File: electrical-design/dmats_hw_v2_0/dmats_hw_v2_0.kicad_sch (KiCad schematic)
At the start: 9 parts, among them J3 Hall_Effect_Sensor_Mod, J4 Hall_Effect_Sensor_Mod, M1 Motor_DC, SW1 RotaryEncoder, U1 ABX00042

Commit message: v2 of circuit for PCB
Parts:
- removed J3, J4: Hall_Effect_Sensor_Mod, symbol Connector:Conn_01x04_Pin
- added U2 (x2): A1324, Package_TH_SIP:SIP-3, symbol custom:A132x
- BT1, BT2, BT3: value Battery_Cell -> 3V7 LI-ION
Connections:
- net +3.3V: now also U1.JD3 (+3V3)
- net +5V: now also U1.JD1 (+5V), U2.1 (VCC), U2.1 (VCC)
- net GND: now also U1.JD4 (GND_2), U2.3 (GND), U2.3 (GND)
- net M1: now also M1.1 (+); no longer M1.2 (-)
- net M2: now also M1.2 (-); no longer M1.1 (+)
- net C1: no longer names the net of U1.JA9 (D0)
- net C1: no longer SW1.C (C1)
- net C2: no longer names the net of U1.JA10 (D1)
- net C2: no longer SW1.B (C2)
- net HES_A1 renamed HES_OUT1
- net HES_OUT1: now also U2.2 (VOUT)
- net HES_A2 renamed HES_OUT2
- net HES_OUT2: now also U2.2 (VOUT)
- net HES_D1 renamed FAULT
- net HES_D2 renamed BLO
- net IN1 renamed AHI
- net IN2 renamed BHI
- net PWM_A renamed ALO
- new net ENC_A: SW1.B (C2)
- new net ENC_B: SW1.C (C1)
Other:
- note added: "5V over 3V3 to give better noise margin"
- note added: "A1324 chosen over A1325, A1326 for it's higher sensivity, better for yes/no sensing"
- moved on the sheet: BT1, BT2, BT3, M1, SW1, U1C, U4

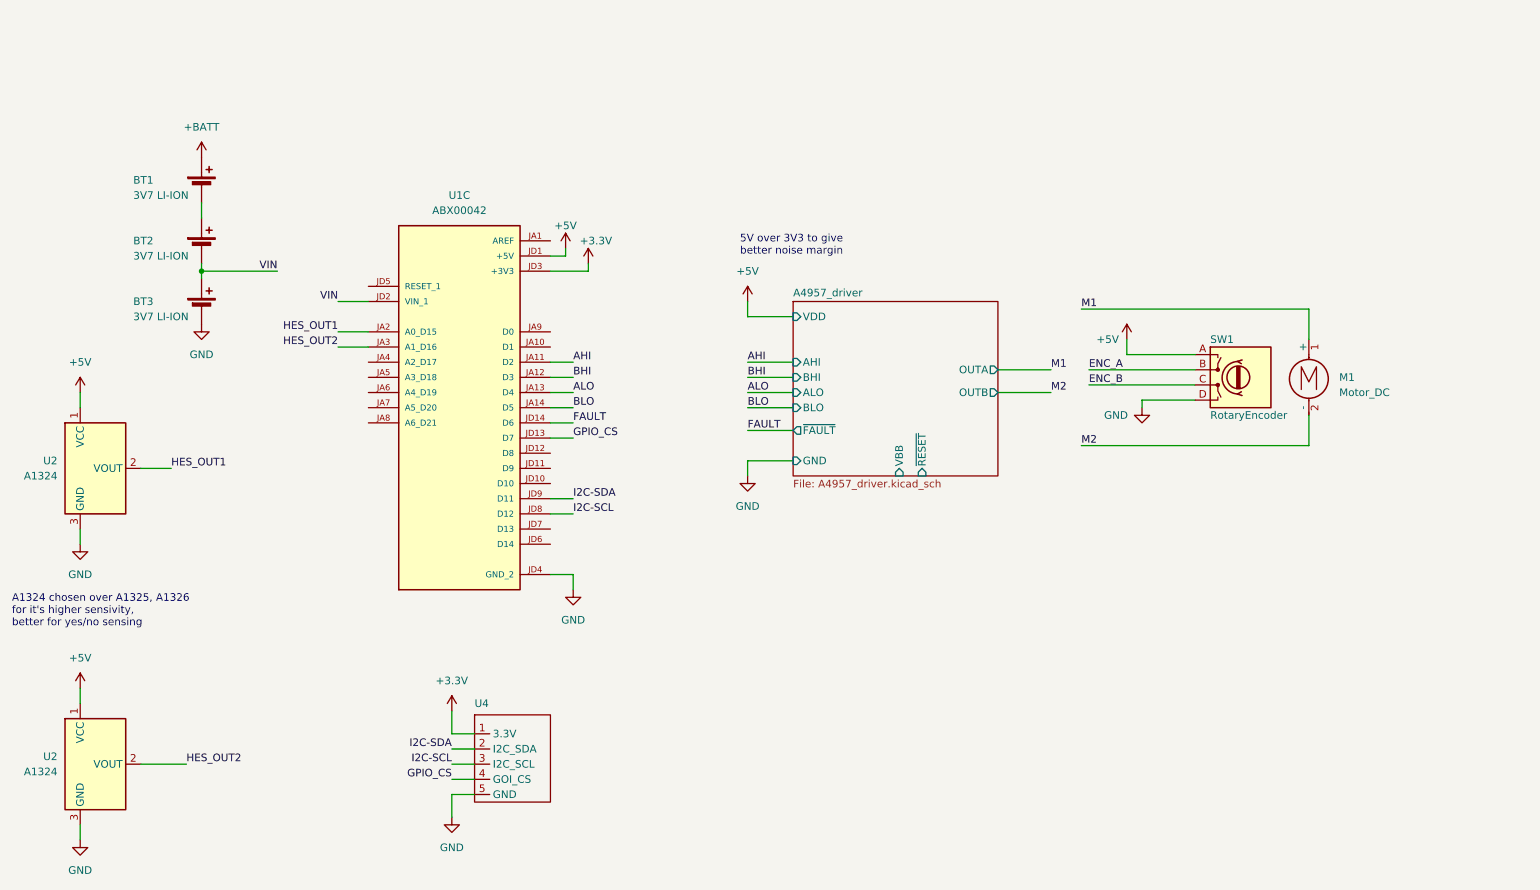
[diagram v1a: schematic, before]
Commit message: created all PCB footprints
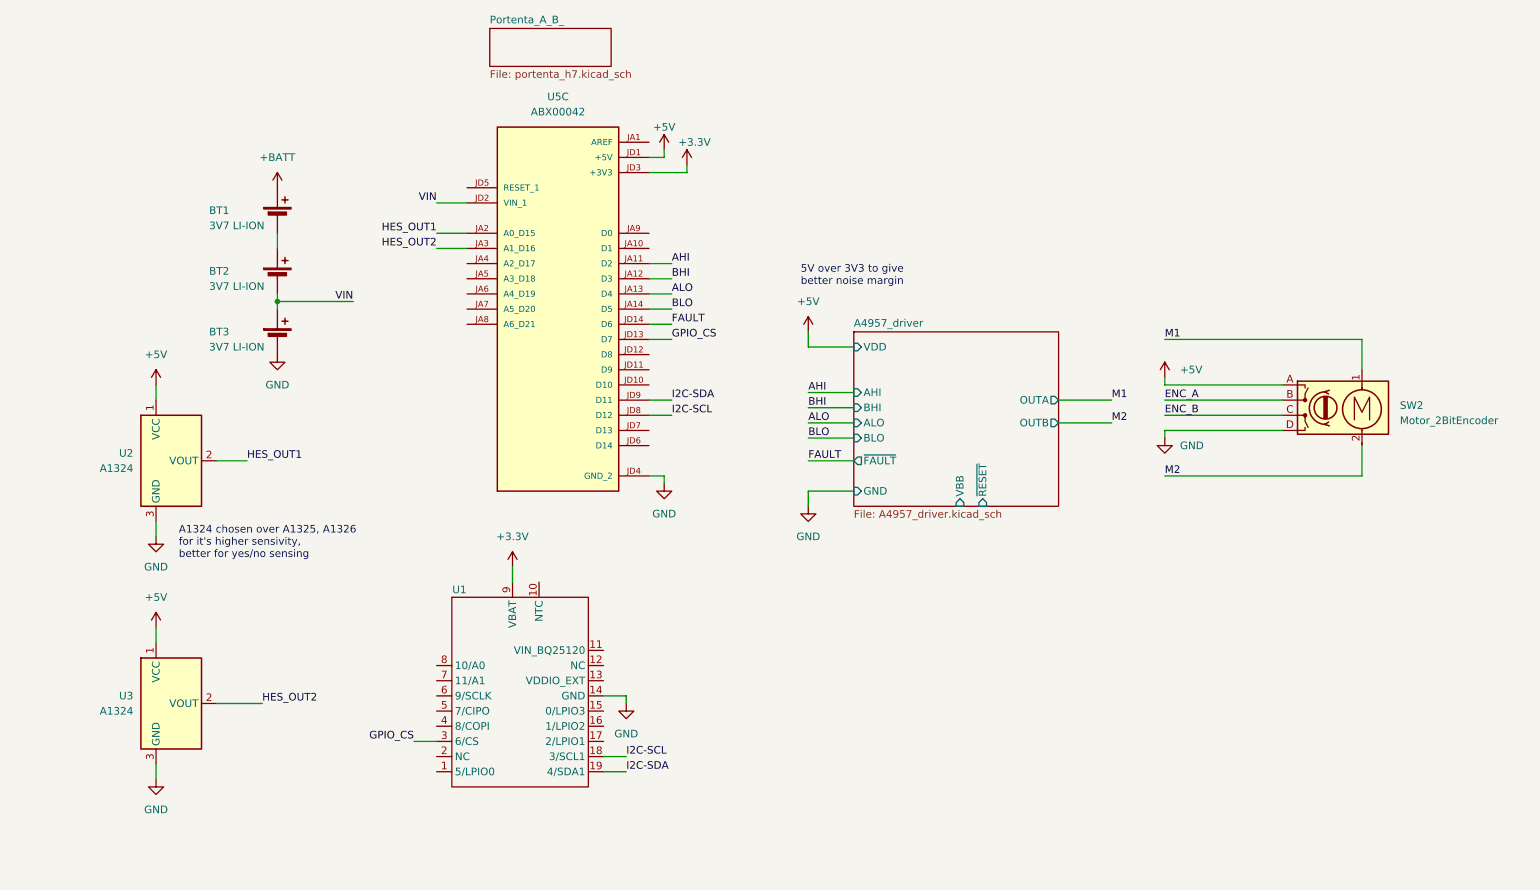
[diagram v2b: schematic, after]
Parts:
- removed M1: Motor_DC, symbol Motor:Motor_DC
- removed SW1: RotaryEncoder, symbol Device:RotaryEncoder
- removed U1: ABX00042, ABX00042:MODULE_ABX00042, symbol ABX00042:ABX00042
- removed U4: ~, symbol custom:NICLA_SENSE_ME
- added SW2: Motor_2BitEncoder, Resistor_SMD:R_0603_1608Metric, symbol DMATS_capstone:Motor_2BitEncoder
- added U1: ~, DMATS_capstone:ARDUINO_NICLA, symbol DMATS_capstone:Nicla_Sense_ME
- added U5: ABX00042, DMATS_capstone:MODULE_ABX00042, symbol DMATS_capstone:ABX00042
- renumbered U2 to U3
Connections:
- net +3.3V: now also U1.9 (VBAT), U5.JD3 (+3V3)
- net +5V: now also SW2.A (VCC), U5.JD1 (+5V)
- net AHI: now also U5.JA11 (D2)
- net ALO: now also U5.JA13 (D4)
- net BHI: now also U5.JA12 (D3)
- net BLO: now also U5.JA14 (D5)
- net ENC_A: now also SW2.B (C2)
- net ENC_B: now also SW2.C (C1)
- net FAULT: now also U5.JD14 (D6)
- net GND: now also SW2.D (GND), U1.14 (GND), U5.JD4 (GND_2)
- net GPIO_CS: now also U1.3 (6/CS), U5.JD13 (D7)
- net HES_OUT1: now also U5.JA2 (A0_D15)
- net HES_OUT2: now also U5.JA3 (A1_D16)
- net I2C-SCL: now also U1.18 (3/SCL1), U5.JD8 (D12)
- net I2C-SDA: now also U1.19 (4/SDA1), U5.JD9 (D11)
- net M1: now also SW2.1 (+)
- net M2: now also SW2.2 (-)
- net VIN: now also U5.JD2 (VIN_1)
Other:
- added sheet Portenta_A_B_ (portenta_h7.kicad_sch)
- moved on the sheet: BT1, BT2, BT3, U2, U3

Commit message: bulk of PCB design layout complete
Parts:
- removed U5: ABX00042, DMATS_capstone:MODULE_ABX00042, symbol DMATS_capstone:ABX00042
- added U4: ABX00042, DMATS_capstone:MODULE_ABX00042, symbol DMATS_capstone:ABX00042
- BT1, BT2, BT3: footprint (none) -> Battery:BatteryHolder_Keystone_1042_1x18650
- SW2: footprint Resistor_SMD:R_0603_1608Metric -> Connector_JST:JST_PH_B6B-PH-K_1x06_P2.00mm_Vertical
- U2, U3: footprint Package_TH_SIP:SIP-3 -> Connector_JST:JST_EH_S3B-EH_1x03_P2.50mm_Horizontal
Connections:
- net +3.3V: now also U4.JD3 (+3V3)
- net +5V: now also SW2.2 (VCC), U4.JD1 (+5V); no longer SW2.A (VCC)
- net AHI: now also U4.JA11 (D2)
- net ALO: now also U4.JA13 (D4)
- net BHI: now also U4.JA12 (D3)
- net BLO: now also U4.JA14 (D5)
- net ENC_A: now also SW2.3 (C2); no longer SW2.B (C2)
- net ENC_B: now also SW2.4 (C1); no longer SW2.C (C1)
- net FAULT: now also U4.JD14 (D6)
- net GND: now also SW2.5 (GND), U4.JD4 (GND_2); no longer SW2.D (GND)
- net GPIO_CS: now also U4.JD13 (D7)
- net HES_OUT1: now also U4.JA2 (A0_D15)
- net HES_OUT2: now also U4.JA3 (A1_D16)
- net I2C-SCL: now also U4.JD8 (D12)
- net I2C-SDA: now also U4.JD9 (D11)
- net M2: now also SW2.6 (M2); no longer SW2.2 (-)
- net VIN: now also U4.JD2 (VIN_1)
- new net: U4.J2_11 (NC_1), U4.J2_13 (NC_1), U4.J2_15 (NC_1), U4.J2_17 (NC_1), U4.J2_19 (NC_1), U4.J2_21 (NC_1), U4.J2_29 (NC_1), U4.J2_30 (NC_1), U4.J2_31 (NC_1), U4.J2_32 (NC_1), U4.J2_35 (NC_1), U4.J2_37 (NC_1), U4.J2_39 (NC_1), U4.J2_41 (NC_1), U4.J2_55 (NC_1), U4.J2_9 (NC_1)
- new net: U4.J2_23 (VCC/+3V3), U4.J2_43 (VCC/+3V3), U4.J2_69 (VCC/+3V3)
- new net: U4.J2_24 (GND_1), U4.J2_33 (GND_1), U4.J2_44 (GND_1), U4.J2_57 (GND_1), U4.J2_70 (GND_1)
- new net: U4.J1_11 (NC), U4.J1_13 (NC), U4.J1_15 (NC), U4.J1_2 (NC), U4.J1_24 (NC), U4.J1_30 (NC), U4.J1_4 (NC), U4.J1_50 (NC), U4.J1_52 (NC), U4.J1_6 (NC), U4.J1_67 (NC), U4.J1_69 (NC), U4.J1_70 (NC), U4.J1_71 (NC), U4.J1_74 (NC), U4.J1_76 (NC), U4.J1_78 (NC), U4.J1_8 (NC), U4.J1_80 (NC), U4.J1_9 (NC)
- new net: U4.J1_21 (VIN), U4.J1_32 (VIN), U4.J1_41 (VIN), U4.J1_48 (VIN)
- new net: U4.J1_22 (GND), U4.J1_31 (GND), U4.J1_42 (GND), U4.J1_47 (GND), U4.J1_54 (GND)
- new net: U4.J1_53 (VSYS), U4.J1_64 (VSYS)
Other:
- removed sheet Portenta_A_B_

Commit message: completed motor driver PCB
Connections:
- net +BATT: now also BT2.1 (+); no longer BT1.1 (+)
- net ALO: now also U4.JA12 (D3); no longer U4.JA13 (D4)
- net BHI: now also U4.JA13 (D4); no longer U4.JA12 (D3)
- net FAULT: now also U4.JA10 (D1); no longer U4.JD14 (D6)
- net VIN: now also BT1.2 (-); no longer BT2.2 (-)
- new net: BT1.1 (+), BT2.2 (-)
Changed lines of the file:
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@@
+    (stroke (width 0.25) (type default))
+  )
+  (wire (pts (xy 144.78 81.28) (xy 144.78 91.44))
     (stroke (width 0.25) (type default))
   )
   (wire (pts (xy 128.27 110.49) (xy 128.27 109.22))
+    (stroke (width 0.25) (type default))
+  )
+  (wire (pts (xy 144.78 91.44) (xy 160.02 91.44))
     (stroke (width 0.25) (type default))
   )
@@
     (stroke (width 0.25) (type default))
   )
-  (wire (pts (xy 125.73 83.82) (xy 129.54 83.82))
-    (stroke (width 0.25) (type default))
-  )
   (wire (pts (xy 43.18 93.98) (xy 43.18 96.52))
     (stroke (width 0.25) (type default))
@@
     (stroke (width 0.25) (type default))
   )
+  (wire (pts (xy 125.73 71.12) (xy 129.54 71.12))
+    (stroke (width 0.25) (type default))
+  )
   (wire (pts (xy 86.36 153.67) (xy 90.17 153.67))
     (stroke (width 0.25) (type default))
@@
     (effects (font (size 1.27 1.27)) (justify left bottom))
   )
-  (label "BHI" (at 129.54 76.2 0) (fields_autoplaced)
-    (effects (font (size 1.27 1.27)) (justify left bottom))
-  )
   (label "M2" (at 212.09 109.22 0) (fields_autoplaced)
     (effects (font (size 1.27 1.27)) (justify left bottom))
@@
     (effects (font (size 1.27 1.27)) (justify right bottom))
   )
-  (label "FAULT" (at 129.54 83.82 0) (fields_autoplaced)
-    (effects (font (size 1.27 1.27)) (justify left bottom))
-  )
   (label "HES_OUT2" (at 60.96 147.32 0) (fields_autoplaced)
     (effects (font (size 1.27 1.27)) (justify left bottom))
   )
   (label "FAULT" (at 152.4 106.68 0) (fields_autoplaced)
+    (effects (font (size 1.27 1.27)) (justify left bottom))
+  )
+  (label "FAULT" (at 129.54 71.12 0) (fields_autoplaced)
     (effects (font (size 1.27 1.27)) (justify left bottom))
   )
@@
     (effects (font (size 1.27 1.27)) (justify left bottom))
   )
+  (label "BHI" (at 129.54 78.74 0) (fields_autoplaced)
+    (effects (font (size 1.27 1.27)) (justify left bottom))
+  )
   (label "I2C-SCL" (at 121.92 156.21 0) (fields_autoplaced)
     (effects (font (size 1.27 1.27)) (justify left bottom))
@@
     (effects (font (size 1.27 1.27)) (justify left bottom))
   )
-  (label "ALO" (at 129.54 78.74 0) (fields_autoplaced)
+  (label "ALO" (at 129.54 76.2 0) (fields_autoplaced)
     (effects (font (size 1.27 1.27)) (justify left bottom))
   )
@@
     )
   )
+  (symbol (lib_id "Device:Battery_Cell") (at 63.5 66.04 0) (unit 1)
+    (in_bom yes) (on_board yes) (dnp no)
+    (property "Reference" "BT2" (at 52.07 64.77 0)
+      (effects (font (size 1.27 1.27)) (justify left))
+    )
+    (property "Value" "3V7 LI-ION" (at 52.07 67.31 0)
+      (effects (font (size 1.27 1.27)) (justify left))
+    )
+    (property "Footprint" "Battery:BatteryHolder_Keystone_1042_1x18650" (at 63.5 64.516 90)
+      (effects (font (size 1.27 1.27)) hide)
+    )
+    (property "Datasheet" "~" (at 63.5 64.516 90)
+      (effects (font (size 1.27 1.27)) hide)
+    )
+    (pin "1")
+    (pin "2")
+    (instances
+      (project "dmats_hw_v2_0"
+        (path "/47782a9e-3834-4fdd-a08d-6cefd0e2f2ff"
+          (reference "BT2") (unit 1)
+        )
+      )
+    )
+  )
   (symbol (lib_id "power:+5V") (at 128.27 54.61 0) (unit 1)
     (in_bom yes) (on_board yes) (dnp no)
@@
         (path "/47782a9e-3834-4fdd-a08d-6cefd0e2f2ff"
           (reference "#PWR011") (unit 1)
+        )
+      )
+    )
+  )
+  (symbol (lib_id "Device:Battery_Cell") (at 63.5 76.2 0) (unit 1)
+    (in_bom yes) (on_board yes) (dnp no)
+    (property "Reference" "BT1" (at 52.07 74.93 0)
+      (effects (font (size 1.27 1.27)) (justify left))
+    )
+    (property "Value" "3V7 LI-ION" (at 52.07 77.47 0)
+      (effects (font (size 1.27 1.27)) (justify left))
+    )
+    (property "Footprint" "Battery:BatteryHolder_Keystone_1042_1x18650" (at 63.5 74.676 90)
+      (effects (font (size 1.27 1.27)) hide)
+    )
+    (property "Datasheet" "~" (at 63.5 74.676 90)
+      (effects (font (size 1.27 1.27)) hide)
+    )
+    (pin "1")
+    (pin "2")
+    (instances
+      (project "dmats_hw_v2_0"
+        (path "/47782a9e-3834-4fdd-a08d-6cefd0e2f2ff"
+          (reference "BT1") (unit 1)
         )
       )
@@
     )
   )
-  (symbol (lib_id "Device:Battery_Cell") (at 63.5 66.04 0) (unit 1)
-    (in_bom yes) (on_board yes) (dnp no)
-    (property "Reference" "BT1" (at 52.07 64.77 0)
-      (effects (font (size 1.27 1.27)) (justify left))
-    )
-    (property "Value" "3V7 LI-ION" (at 52.07 67.31 0)
-      (effects (font (size 1.27 1.27)) (justify left))
-    )
-    (property "Footprint" "Battery:BatteryHolder_Keystone_1042_1x18650" (at 63.5 64.516 90)
-      (effects (font (size 1.27 1.27)) hide)
-    )
-    (property "Datasheet" "~" (at 63.5 64.516 90)
-      (effects (font (size 1.27 1.27)) hide)
-    )
-    (pin "1")
-    (pin "2")
-    (instances
-      (project "dmats_hw_v2_0"
-        (path "/47782a9e-3834-4fdd-a08d-6cefd0e2f2ff"
-          (reference "BT1") (unit 1)
+  (symbol (lib_id "power:+BATT") (at 144.78 81.28 0) (unit 1)
+    (in_bom yes) (on_board yes) (dnp no) (fields_autoplaced)
+    (property "Reference" "#PWR016" (at 144.78 85.09 0)
+      (effects (font (size 1.27 1.27)) hide)
+    )
+    (property "Value" "+BATT" (at 144.78 76.2 0)
+      (effects (font (size 1.27 1.27)))
+    )
+    (property "Footprint" "" (at 144.78 81.28 0)
+      (effects (font (size 1.27 1.27)) hide)
+    )
+    (property "Datasheet" "" (at 144.78 81.28 0)
+      (effects (font (size 1.27 1.27)) hide)
+    )
+    (pin "1")
+    (instances
+      (project "dmats_hw_v2_0"
+        (path "/47782a9e-3834-4fdd-a08d-6cefd0e2f2ff"
+          (reference "#PWR016") (unit 1)
         )
       )
@@
         (path "/47782a9e-3834-4fdd-a08d-6cefd0e2f2ff"
           (reference "#PWR04") (unit 1)
-        )
-      )
-    )
-  )
-  (symbol (lib_id "Device:Battery_Cell") (at 63.5 76.2 0) (unit 1)
-    (in_bom yes) (on_board yes) (dnp no)
-    (property "Reference" "BT2" (at 52.07 74.93 0)
-      (effects (font (size 1.27 1.27)) (justify left))
-    )
-    (property "Value" "3V7 LI-ION" (at 52.07 77.47 0)
-      (effects (font (size 1.27 1.27)) (justify left))
-    )
-    (property "Footprint" "Battery:BatteryHolder_Keystone_1042_1x18650" (at 63.5 74.676 90)
-      (effects (font (size 1.27 1.27)) hide)
-    )
-    (property "Datasheet" "~" (at 63.5 74.676 90)
-      (effects (font (size 1.27 1.27)) hide)
-    )
-    (pin "1")
-    (pin "2")
-    (instances
-      (project "dmats_hw_v2_0"
-        (path "/47782a9e-3834-4fdd-a08d-6cefd0e2f2ff"
-          (reference "BT2") (unit 1)
         )
       )
@@
       (effects (font (size 1.27 1.27)) (justify left))
     )
-    (pin "VBB" input (at 177.8 114.3 270)
-      (effects (font (size 1.27 1.27) (color 194 0 0 1)) (justify left))
+    (pin "VBB" input (at 160.02 91.44 180)
+      (effects (font (size 1.27 1.27)) (justify left))
     )
     (pin "AHI" input (at 160.02 95.25 180)

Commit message: sim updates for force analysis and visual clean up on elec drawings
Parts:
- added BZ1, BZ2: Buzzer, Buzzer_Beeper:Buzzer_12x9.5RM7.6, symbol Device:Buzzer
- added R3, R4: 10k, Resistor_SMD:R_0603_1608Metric, symbol Device:R
- added SW1: SW_SPST, DMATS_capstone:SW_DIP_SPSTx01_Slide_Power, symbol Switch:SW_SPST
- added SW2, SW3, SW4: SW_SPDT, DMATS_capstone:CUI_SLW-913535-2A-RA-D_SPDT_Angled, symbol Switch:SW_SPDT
- renumbered SW2 to M1
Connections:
- net +5V: now also R3.1, R4.1
- net +BATT: now also BT1.1 (+); no longer BT2.1 (+)
- net GND: now also BZ1.2 (+), BZ2.2 (+)
- net VIN: now also SW2.1 (A); no longer BT1.2 (-), BT3.1 (+)
- net at BT2.2 (-): now also BT3.1 (+), SW2.2 (B); no longer BT1.1 (+)
- net SW_A: now reaches U4.JA4 (A2_D17)
- net SW_A: now also SW3.1 (A)
- net SW_B: now reaches U4.JA5 (A3_D18)
- net SW_B: now also SW3.3 (C)
- net SW_C: now reaches U4.JA6 (A4_D19)
- net SW_C: now also SW4.1 (A)
- net SW_D: now reaches U4.JA7 (A5_D20)
- net SW_D: now also SW4.3 (C)
- net BZ_B: now reaches U4.JD11 (D9)
- net BZ_B: now also BZ2.1 (-)
- net BZ_A: now reaches U4.JD12 (D8)
- net BZ_A: now also BZ1.1 (-)
- new net: BT1.2 (-), SW1.1 (A)
- new net: BT2.1 (+), SW1.2 (B)
- new net: R4.2, SW4.2 (B)
- new net: R3.2, SW3.2 (B)
- new net NC: SW2.3 (C)
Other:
- note added: "5V chosen over 3V3 to give better noise margin"
- note added: "A1324 chosen over A1325, A1326 for it's higher sensivity, better for yes/no read"
- note removed: "5V over 3V3 to give better noise margin"
- note removed: "A1324 chosen over A1325, A1326 for it's higher sensivity, better for yes/no sensing"
- moved on the sheet: M1, U1, U2, U3, U4A, U4B, U4C
